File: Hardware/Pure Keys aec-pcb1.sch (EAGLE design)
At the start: 58 parts, among them IC1 TL074P, IC2 TL072P, IC5 TL074P, Q2 20MHz, T1 2N3904, U2 LM4040A50IDBZT, U3 328P

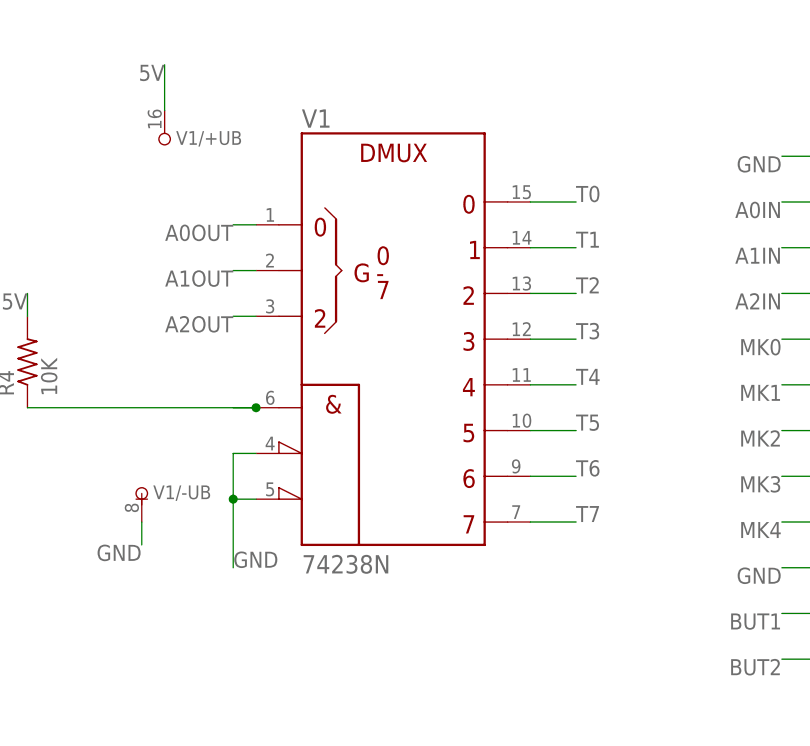
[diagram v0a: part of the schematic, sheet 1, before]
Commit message: changed 74238 for 74138
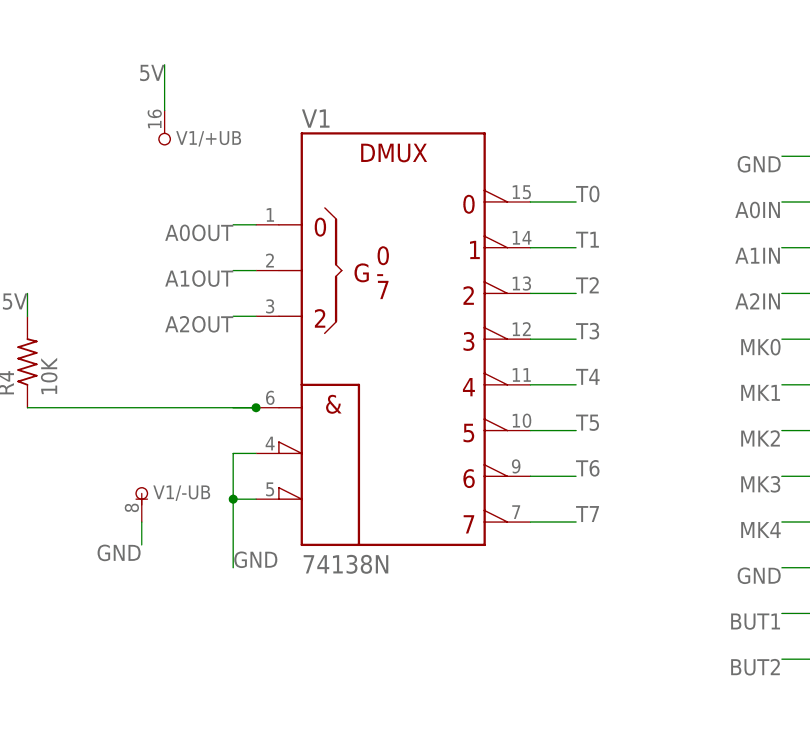
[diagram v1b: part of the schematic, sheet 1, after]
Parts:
- V1: value 74238N -> 74138N; device 74ttl-din:74238N -> 74ttl-din:74138N
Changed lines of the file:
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@@
 <part name="IC2" library="GMSN" deviceset="TL072" device="P" value="TL072P"/>
 <part name="C16" library="rcl" deviceset="C-US" device="C0805K" value="100n"/>
-<part name="V1" library="74ttl-din" library_urn="urn:adsk.eagle:library:84" deviceset="74*238" device="N" package3d_urn="urn:adsk.eagle:package:1462/1"/>
+<part name="V1" library="74ttl-din" library_urn="urn:adsk.eagle:library:84" deviceset="74*138" device="N" package3d_urn="urn:adsk.eagle:package:1462/1"/>
 <part name="V2" library="74ttl-din" library_urn="urn:adsk.eagle:library:84" deviceset="74*151" device="N" package3d_urn="urn:adsk.eagle:package:1462/1"/>
 <part name="U3" library="SparkFun-IC-Microcontroller" deviceset="ATMEGA328P_PDIP" device="" value="328P"/>
